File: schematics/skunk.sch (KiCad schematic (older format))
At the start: 43 parts

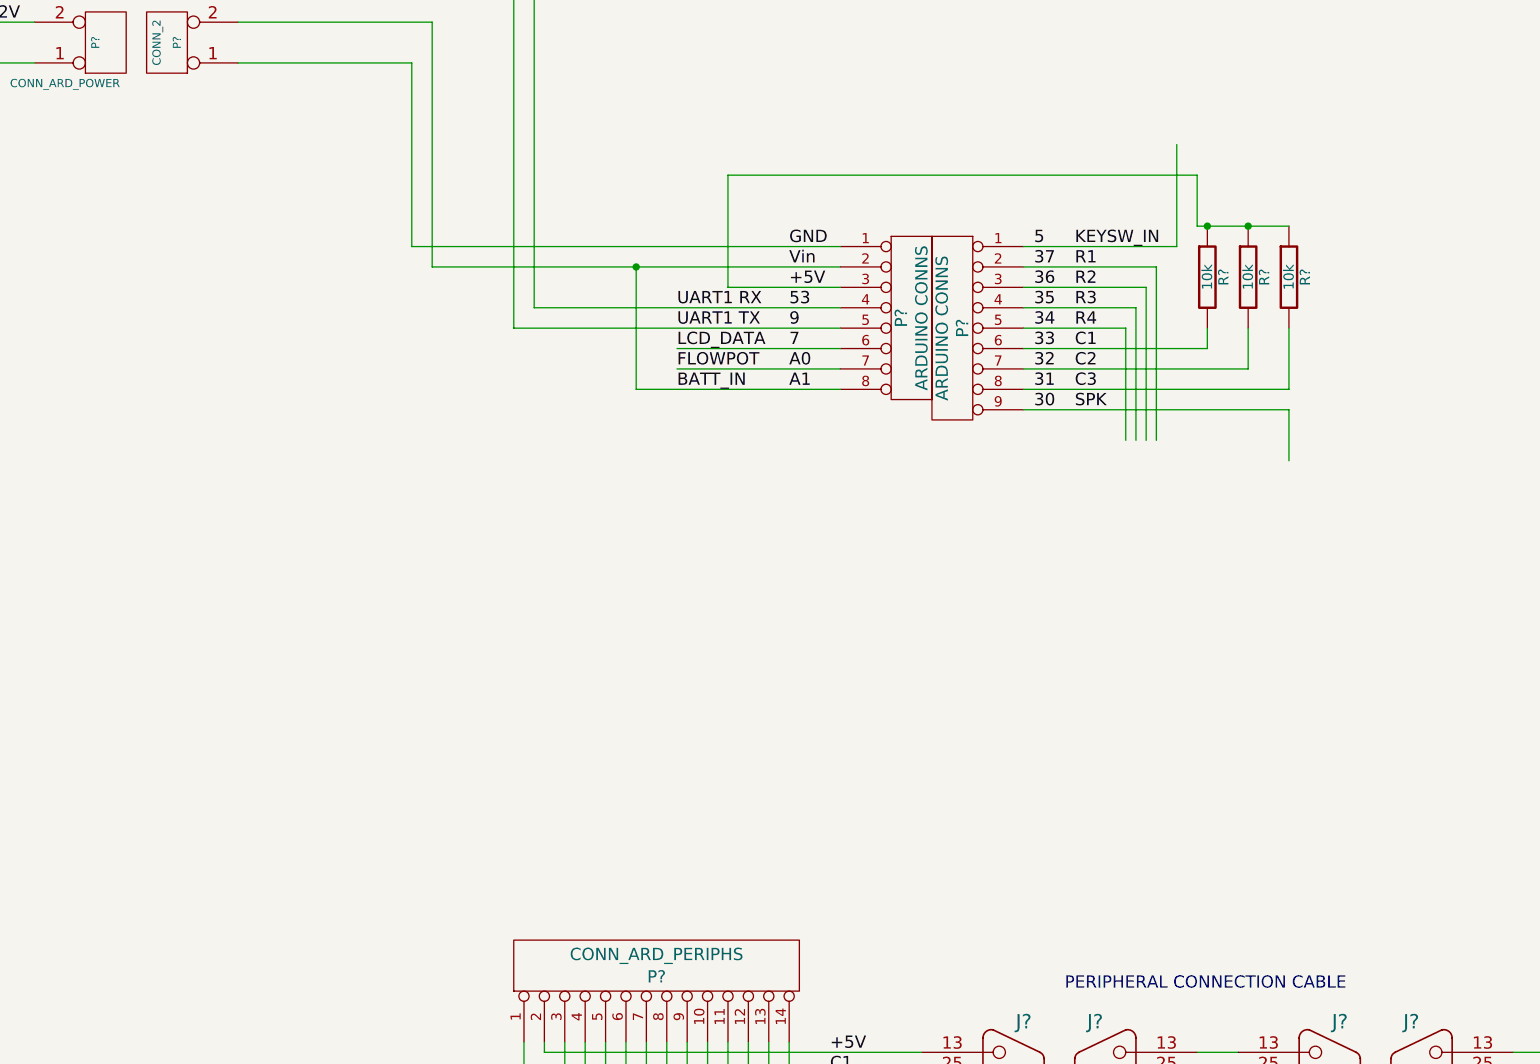
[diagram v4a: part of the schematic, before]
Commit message: Updated TODO and finished most peripheral interface electronics
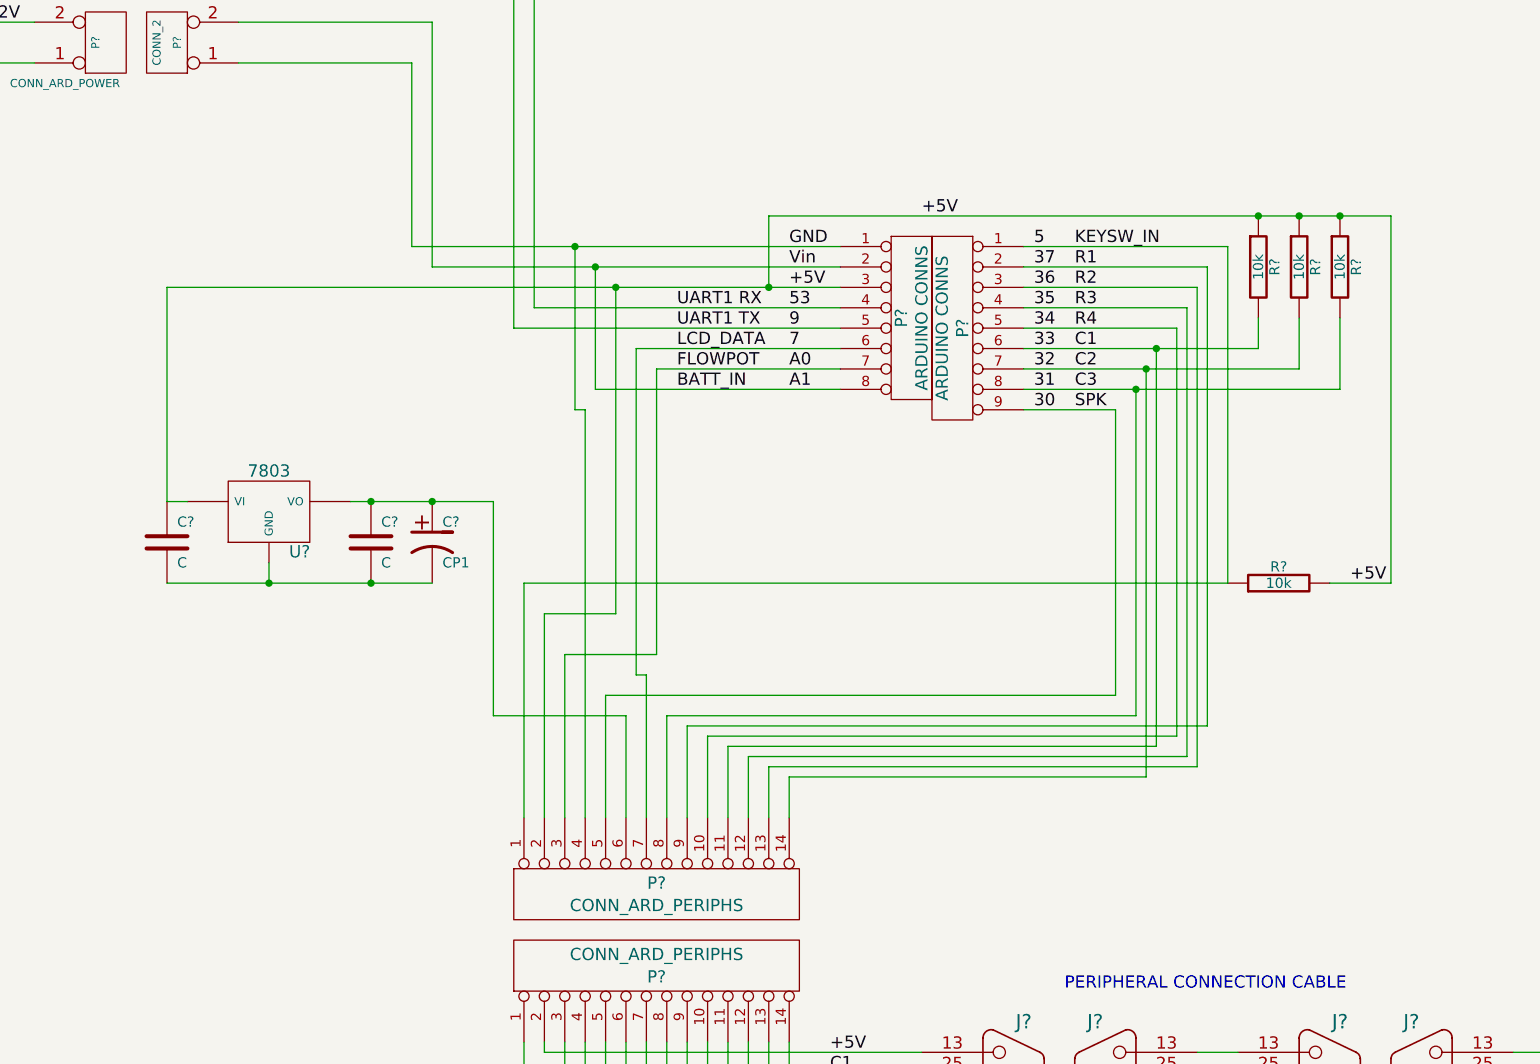
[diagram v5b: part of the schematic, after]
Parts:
- added C? (x2): C, symbol C
- added C?: CP1, symbol CP1
- added P?: CONN_ARD_PERIPHS, symbol CONN_14
- added R?: 10k, symbol R
- added U?: 7803, symbol 7805
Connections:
- wire segments 209 -> 250
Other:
- moved on the sheet: R?
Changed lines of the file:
@@
-EESchema Schematic File Version 2  date Fri 05 Oct 2012 19:54:39 BST
+EESchema Schematic File Version 2  date Fri 05 Oct 2012 20:15:41 BST
 LIBS:power
 LIBS:device
@@
 	4350 4400 6350 4400
 Wire Wire Line
-	5800 4500 6350 4500
-Wire Wire Line
 	4850 4600 6350 4600
 Wire Wire Line
-	5550 4800 6350 4800
-Wire Wire Line
-	5550 4900 6350 4900
-Wire Wire Line
-	5350 5000 6350 5000
-Wire Wire Line
-	7250 4300 8000 4300
-Wire Wire Line
-	7250 4400 7900 4400
-Wire Wire Line
-	7250 4500 7850 4500
-Wire Wire Line
-	7250 4600 7800 4600
-Wire Wire Line
-	7250 4700 7750 4700
-Wire Wire Line
-	7250 4800 8150 4800
-Wire Wire Line
-	7250 4900 8350 4900
-Wire Wire Line
-	7250 5000 8550 5000
+	5350 4800 6350 4800
+Wire Wire Line
+	5450 4900 6350 4900
+Wire Wire Line
+	7250 4400 8150 4400
+Wire Wire Line
+	7250 4500 8100 4500
+Wire Wire Line
+	7250 4600 8050 4600
+Wire Wire Line
+	7250 4700 8000 4700
+Wire Wire Line
+	7250 4800 8400 4800
+Wire Wire Line
+	7250 4900 8600 4900
+Wire Wire Line
+	7250 5000 8800 5000
 Text Label 5550 4600 0    60   ~ 0
 UART1 RX
@@
 C3
 Wire Wire Line
-	5800 4500 5800 3950
-Wire Wire Line
-	5800 3950 8100 3950
-Wire Wire Line
-	7750 4700 7750 5250
-Wire Wire Line
-	7800 4600 7800 5250
-Wire Wire Line
-	7850 4500 7850 5250
-Wire Wire Line
-	7900 4400 7900 5250
-Wire Wire Line
-	8150 4800 8150 4700
+	8400 4800 8400 4650
 $Comp
 L R R?
 U 1 1 506F6F28
-P 8150 4450
-F 0 "R?" V 8230 4450 50  0000 C CNN
-F 1 "10k" V 8150 4450 50  0000 C CNN
-	1    8150 4450
+P 8400 4400
+F 0 "R?" V 8480 4400 50  0000 C CNN
+F 1 "10k" V 8400 4400 50  0000 C CNN
+	1    8400 4400
 	1    0    0    -1
 $EndComp
@@
 L R R?
 U 1 1 506F6F37
-P 8350 4450
-F 0 "R?" V 8430 4450 50  0000 C CNN
-F 1 "10k" V 8350 4450 50  0000 C CNN
-	1    8350 4450
+P 8600 4400
+F 0 "R?" V 8680 4400 50  0000 C CNN
+F 1 "10k" V 8600 4400 50  0000 C CNN
+	1    8600 4400
 	1    0    0    -1
 $EndComp
@@
 L R R?
 U 1 1 506F6F46
-P 8550 4450
-F 0 "R?" V 8630 4450 50  0000 C CNN
-F 1 "10k" V 8550 4450 50  0000 C CNN
-	1    8550 4450
-	1    0    0    -1
-$EndComp
-Connection ~ 8150 4200
-Connection ~ 8350 4200
-Wire Wire Line
-	8350 4900 8350 4700
-Wire Wire Line
-	8550 5000 8550 4700
-Wire Wire Line
-	8000 4300 8000 3800
-Wire Wire Line
-	8100 3950 8100 4200
-Wire Wire Line
-	8100 4200 8550 4200
-Wire Wire Line
-	5350 4400 5350 5000
+P 8800 4400
+F 0 "R?" V 8880 4400 50  0000 C CNN
+F 1 "10k" V 8800 4400 50  0000 C CNN
+	1    8800 4400
+	1    0    0    -1
+$EndComp
+Wire Wire Line
+	8600 4900 8600 4650
+Wire Wire Line
+	8800 5000 8800 4650
 Text Label 13100 8400 0    60   ~ 0
 SPK
@@
 Wire Wire Line
 	4350 3200 4350 4400
-Connection ~ 5350 4400
 Text Label 6300 8250 0    60   ~ 0
 +5V
@@
 	-1   0    0    -1
 $EndComp
-Wire Wire Line
-	7250 5100 8550 5100
-Wire Wire Line
-	8550 5100 8550 5350
 Text Label 7300 5100 0    60   ~ 0
 30
 Text Label 7500 5100 0    60   ~ 0
 SPK
+Wire Wire Line
+	5450 4900 5450 6300
+Wire Wire Line
+	6350 5000 5150 5000
+Wire Wire Line
+	5150 5000 5150 4400
+Connection ~ 5150 4400
+Wire Wire Line
+	6000 4150 9050 4150
+Connection ~ 8600 4150
+Connection ~ 8400 4150
+Wire Wire Line
+	7250 5100 7700 5100
+Wire Wire Line
+	7700 5100 7700 6500
+Wire Wire Line
+	7800 5000 7800 6600
+Connection ~ 7800 5000
+Wire Wire Line
+	7850 4900 7850 6900
+Connection ~ 7850 4900
+Wire Wire Line
+	7900 4800 7900 6750
+Connection ~ 7900 4800
+Wire Wire Line
+	8000 4700 8000 6700
+Wire Wire Line
+	8050 4600 8050 6800
+Wire Wire Line
+	8150 4400 8150 6650
+Wire Wire Line
+	7250 4300 8250 4300
+Wire Wire Line
+	8250 4300 8250 5950
+Wire Wire Line
+	3050 4500 6350 4500
+Wire Wire Line
+	6000 4500 6000 4150
+Wire Wire Line
+	5350 4800 5350 6400
+$Comp
+L CONN_14 P?
+U 1 1 506FE3B5
+P 5450 7450
+F 0 "P?" V 5420 7450 60  0000 C CNN
+F 1 "CONN_ARD_PERIPHS" V 5530 7450 60  0000 C CNN
+	1    5450 7450
+	0    -1   1    0
+$EndComp
+Wire Wire Line
+	4800 5950 4800 7100
+Wire Wire Line
+	5250 4500 5250 6100
+Wire Wire Line
+	5250 6100 4900 6100
+Wire Wire Line
+	4900 6100 4900 7100
+Connection ~ 6000 4500
+Wire Wire Line
+	5000 7100 5000 6300
+Wire Wire Line
+	5000 6300 5450 6300
+Wire Wire Line
+	5400 7100 5400 6400
+Wire Wire Line
+	5400 6400 5350 6400
+Wire Wire Line
+	5100 7100 5100 5100
+Wire Wire Line
+	5100 5100 5050 5100
+Wire Wire Line
+	5050 5100 5050 4300
+Connection ~ 5050 4300
+Wire Wire Line
+	7700 6500 5200 6500
+Wire Wire Line
+	5200 6500 5200 7100
+$Comp
+L 7805 U?
+U 1 1 506FEDD2
+P 3550 5600
+F 0 "U?" H 3700 5404 60  0000 C CNN
+F 1 "7803" H 3550 5800 60  0000 C CNN
+	1    3550 5600
+	1    0    0    -1
+$EndComp
+$Comp
+L C C?
+U 1 1 506FEDF0
+P 3050 5750
+F 0 "C?" H 3100 5850 50  0000 L CNN
+F 1 "C" H 3100 5650 50  0000 L CNN
+	1    3050 5750
+	1    0    0    -1
+$EndComp
+$Comp
+L C C?
+U 1 1 506FEDFF
+P 4050 5750
+F 0 "C?" H 4100 5850 50  0000 L CNN
+F 1 "C" H 4100 5650 50  0000 L CNN
+	1    4050 5750
+	1    0    0    -1
+$EndComp
+$Comp
+L CP1 C?
+U 1 1 506FEE0E
+P 4350 5750
+F 0 "C?" H 4400 5850 50  0000 L CNN
+F 1 "CP1" H 4400 5650 50  0000 L CNN
+	1    4350 5750
+	1    0    0    -1
+$EndComp
+Wire Wire Line
+	3050 5950 4350 5950
+Connection ~ 4050 5950
+Wire Wire Line
+	3050 5550 3150 5550
+Wire Wire Line
+	3950 5550 4650 5550
+Connection ~ 4050 5550
+Wire Wire Line
+	3050 5550 3050 4500
+Connection ~ 5250 4500
+Wire Wire Line
+	5300 7100 5300 6600
+Wire Wire Line
+	5300 6600 4650 6600
+Wire Wire Line
+	4650 6600 4650 5550
+Connection ~ 4350 5550
+Wire Wire Line
+	7800 6600 5500 6600
+Wire Wire Line
+	5500 6600 5500 7100
+Wire Wire Line
+	5600 7100 5600 6650
+Wire Wire Line
+	5600 6650 8150 6650
+Wire Wire Line
+	5700 7100 5700 6700
+Wire Wire Line
+	5700 6700 8000 6700
+Wire Wire Line
+	5800 7100 5800 6750
+Wire Wire Line
+	5800 6750 7900 6750
+Wire Wire Line
+	5900 7100 5900 6800
+Wire Wire Line
+	5900 6800 8050 6800
+Wire Wire Line
+	6000 7100 6000 6850
+Wire Wire Line
+	6000 6850 8100 6850
+Wire Wire Line
+	8100 6850 8100 4500
+Wire Wire Line
+	6100 7100 6100 6900
+Wire Wire Line
+	6100 6900 7850 6900
+Wire Wire Line
+	8250 5950 4800 5950
+$Comp
+L R R?
+U 1 1 5070099C
+P 8500 5950
+F 0 "R?" V 8580 5950 50  0000 C CNN
+F 1 "10k" V 8500 5950 50  0000 C CNN
+	1    8500 5950
+	0    -1   -1   0
+$EndComp
+Wire Wire Line
+	9050 4150 9050 5950
+Wire Wire Line
+	9050 5950 8750 5950
+Connection ~ 8800 4150
+Text Label 6750 4150 0    60   ~ 0
++5V
+Text Label 8850 5950 0    60   ~ 0
++5V
+Wire Wire Line
+	3550 5850 3550 5950
+Connection ~ 3550 5950
 $EndSCHEMATC

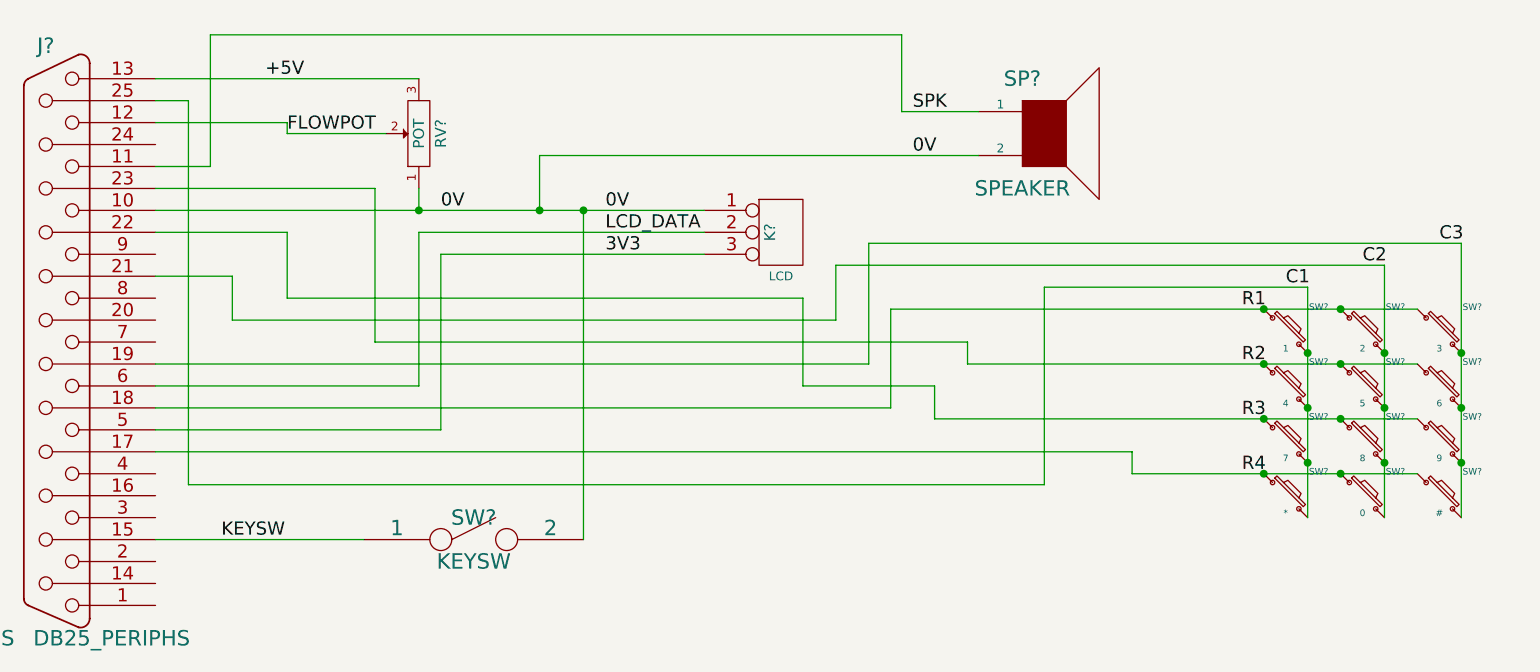
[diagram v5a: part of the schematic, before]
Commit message: Added LCD clamp diode current limit resistor
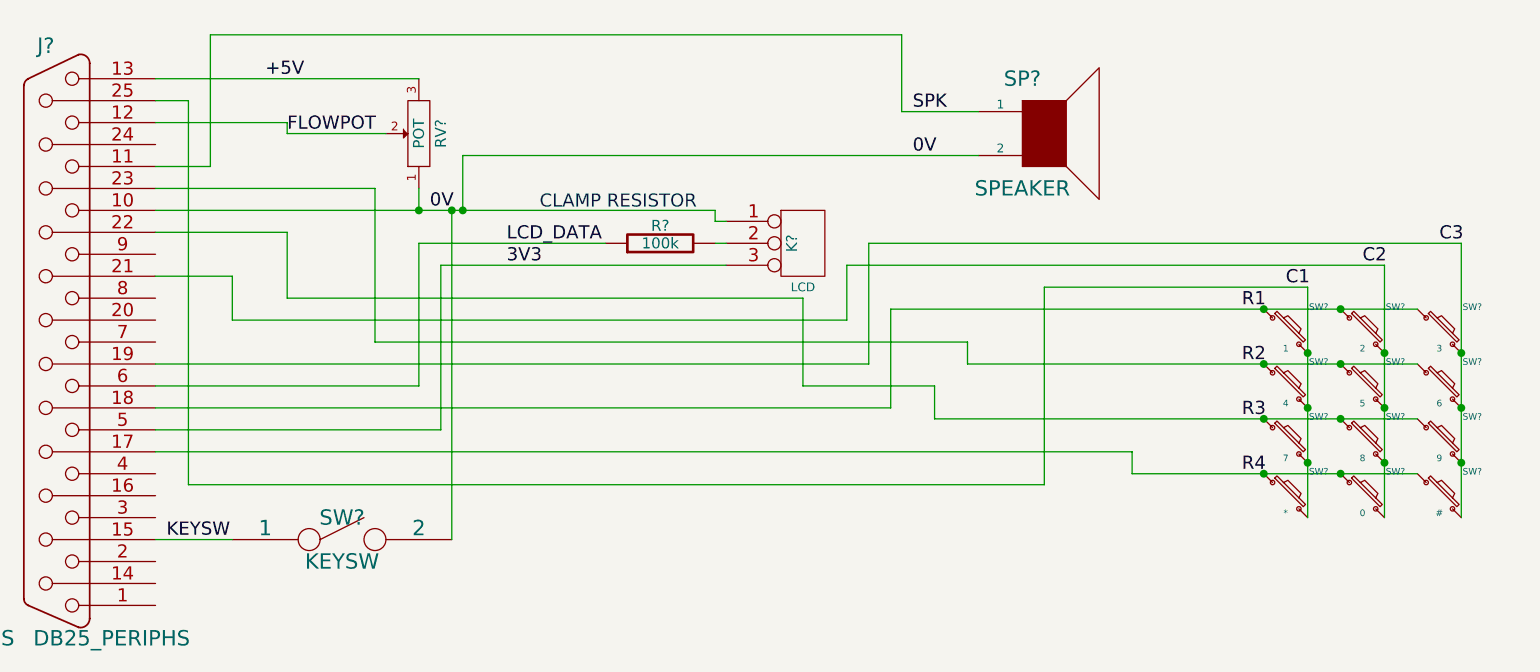
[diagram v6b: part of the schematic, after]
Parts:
- added R?: 100k, symbol R
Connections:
- net 7: now also R?.1; no longer K?.2 (PM)
- new net: K?.2 (PM), R?.2
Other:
- note added: "CLAMP RESISTOR"
- moved on the sheet: K?, SW?
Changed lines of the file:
@@
-EESchema Schematic File Version 2  date Fri 05 Oct 2012 20:15:41 BST
+EESchema Schematic File Version 2  date Mon 15 Oct 2012 14:20:48 BST
 LIBS:power
 LIBS:device
@@
 Sheet 1 1
 Title "SKUNK WIRING HARNESS AND SCHEMATIC"
-Date "5 oct 2012"
+Date "15 oct 2012"
 Rev ""
 Comp "CAMBRIDGE UNIVERSITY SPACE FLIGHT - dwt27"
@@
 Text Label 13100 8600 0    60   ~ 0
 0V
-Text Label 11700 8950 0    60   ~ 0
+Text Label 11250 9000 0    60   ~ 0
 LCD_DATA
-Text Label 11700 9050 0    60   ~ 0
+Text Label 11250 9100 0    60   ~ 0
 3V3
-Text Label 11700 8850 0    60   ~ 0
-0V
 Text Label 10150 8250 0    60   ~ 0
 +5V
-Text Label 10950 8850 0    60   ~ 0
+Text Label 10900 8850 0    60   ~ 0
 0V
 $Comp
 L SPST SW?
 U 1 1 50638E78
-P 11100 10350
-F 0 "SW?" H 11100 10450 70  0000 C CNN
-F 1 "KEYSW" H 11100 10250 70  0000 C CNN
-	1    11100 10350
+P 10500 10350
+F 0 "SW?" H 10500 10450 70  0000 C CNN
+F 1 "KEYSW" H 10500 10250 70  0000 C CNN
+	1    10500 10350
 	1    0    0    -1
 $EndComp
@@
 L CONN_3 K?
 U 1 1 50637AB3
-P 12500 8950
-F 0 "K?" V 12450 8950 50  0000 C CNN
-F 1 "LCD" H 12500 8750 40  0000 C CNN
-	1    12500 8950
+P 12600 9000
+F 0 "K?" V 12550 9000 50  0000 C CNN
+F 1 "LCD" H 12600 8800 40  0000 C CNN
+	1    12600 9000
 	1    0    0    -1
 $EndComp
@@
 Wire Wire Line
 	12900 9550 9650 9550
-Connection ~ 11400 8850
-Wire Wire Line
-	13400 8600 11400 8600
-Wire Wire Line
-	11400 8600 11400 8850
-Wire Wire Line
-	12150 9050 10950 9050
-Wire Wire Line
-	10950 9050 10950 9850
+Wire Wire Line
+	11050 8600 13400 8600
 Wire Wire Line
 	10950 9850 9650 9850
 Connection ~ 10850 8850
-Wire Wire Line
-	11600 8850 11600 10350
 Wire Wire Line
 	9650 8250 10850 8250
@@
 	10850 8850 10850 8750
 Wire Wire Line
-	9650 10350 10600 10350
-Wire Wire Line
-	12150 8850 9650 8850
-Connection ~ 11600 8850
-Wire Wire Line
 	9650 9650 10850 9650
 Wire Wire Line
-	10850 9650 10850 8950
-Wire Wire Line
-	10850 8950 12150 8950
-Wire Wire Line
 	9650 8650 9900 8650
 Wire Wire Line
@@
 	10000 9150 10000 9350
 Wire Wire Line
-	10000 9350 12750 9350
-Wire Wire Line
-	12750 9350 12750 9100
-Wire Wire Line
-	12750 9100 15250 9100
+	10000 9350 12800 9350
 Wire Wire Line
 	9650 8750 10650 8750
@@
 Text Label 10250 8500 0    60   ~ 0
 FLOWPOT
-Text Label 9950 10350 0    60   ~ 0
+Text Label 9700 10350 0    60   ~ 0
 KEYSW
 Wire Wire Line
@@
 	3550 5850 3550 5950
 Connection ~ 3550 5950
+$Comp
+L R R?
+U 1 1 507C15C2
+P 11950 9000
+F 0 "R?" V 12030 9000 50  0000 C CNN
+F 1 "100k" V 11950 9000 50  0000 C CNN
+	1    11950 9000
+	0    -1   -1   0
+$EndComp
+Wire Wire Line
+	9650 10350 10000 10350
+Wire Wire Line
+	11000 10350 11000 8850
+Connection ~ 11000 8850
+Wire Wire Line
+	11050 8850 11050 8600
+Connection ~ 11050 8850
+Wire Wire Line
+	15250 9100 12800 9100
+Wire Wire Line
+	12800 9100 12800 9350
+Wire Wire Line
+	10950 9850 10950 9100
+Wire Wire Line
+	10950 9100 12250 9100
+Wire Wire Line
+	12200 9000 12250 9000
+Wire Wire Line
+	10850 9650 10850 9000
+Wire Wire Line
+	10850 9000 11700 9000
+Wire Wire Line
+	9650 8850 12200 8850
+Wire Wire Line
+	12200 8850 12200 8900
+Wire Wire Line
+	12200 8900 12250 8900
+Text Notes 11400 8850 0    60   ~ 0
+CLAMP RESISTOR
 $EndSCHEMATC
